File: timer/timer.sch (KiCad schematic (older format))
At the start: 23 parts, among them J1 Conn_01x02_Female, Q1 BC546, Q2 BC546, U1 LM339, U2 7402

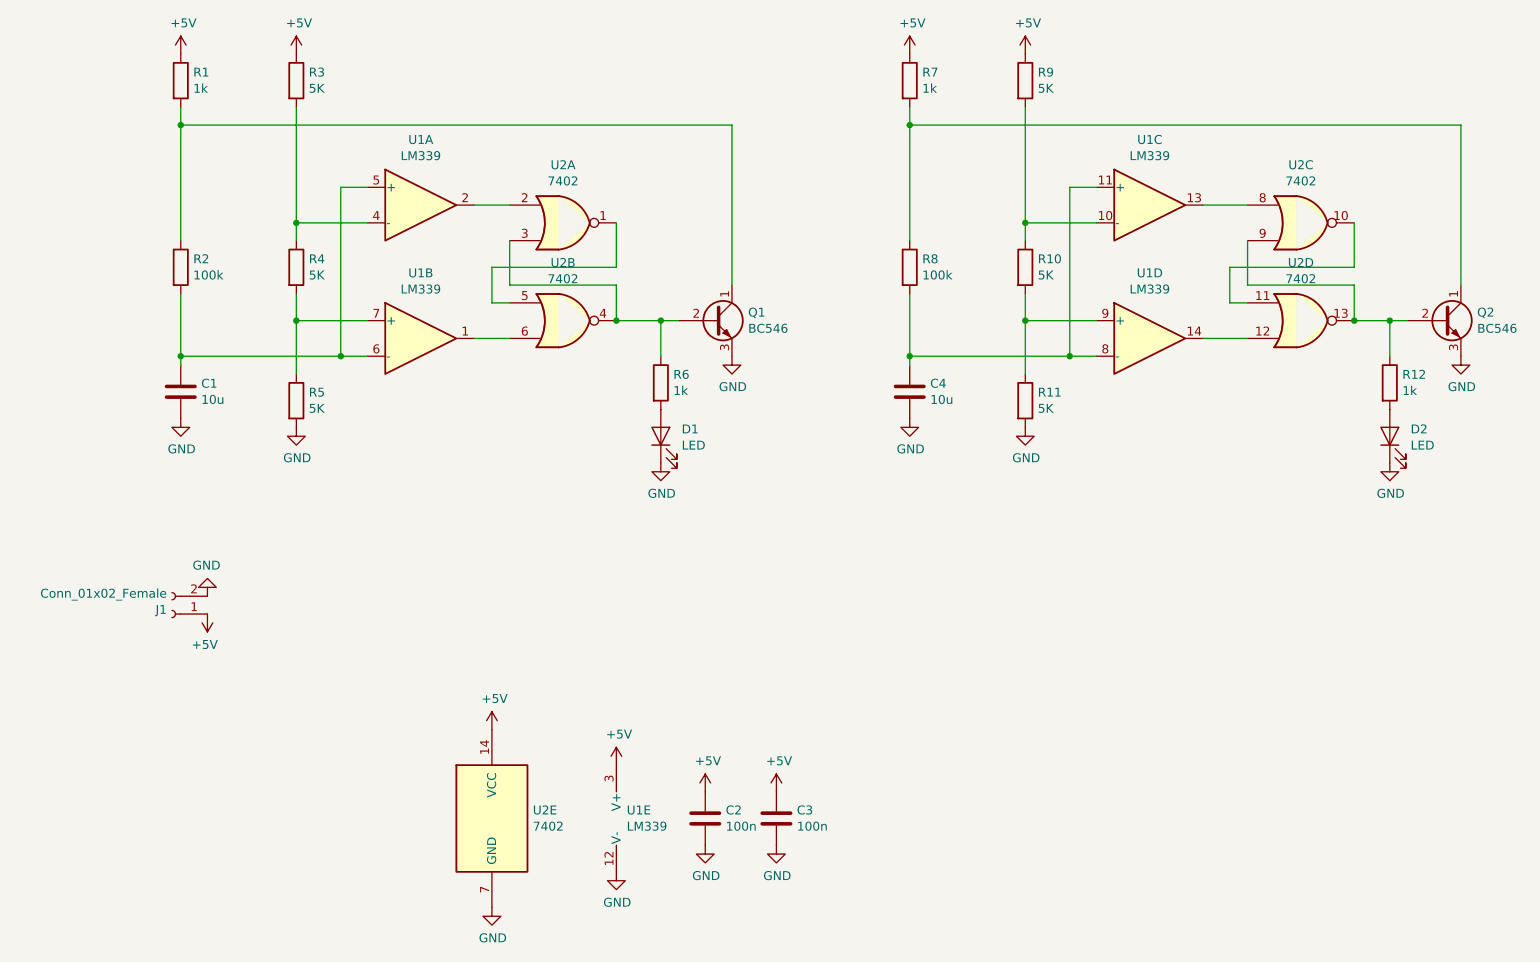
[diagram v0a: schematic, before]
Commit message: Start using opamp that can ouput stuff
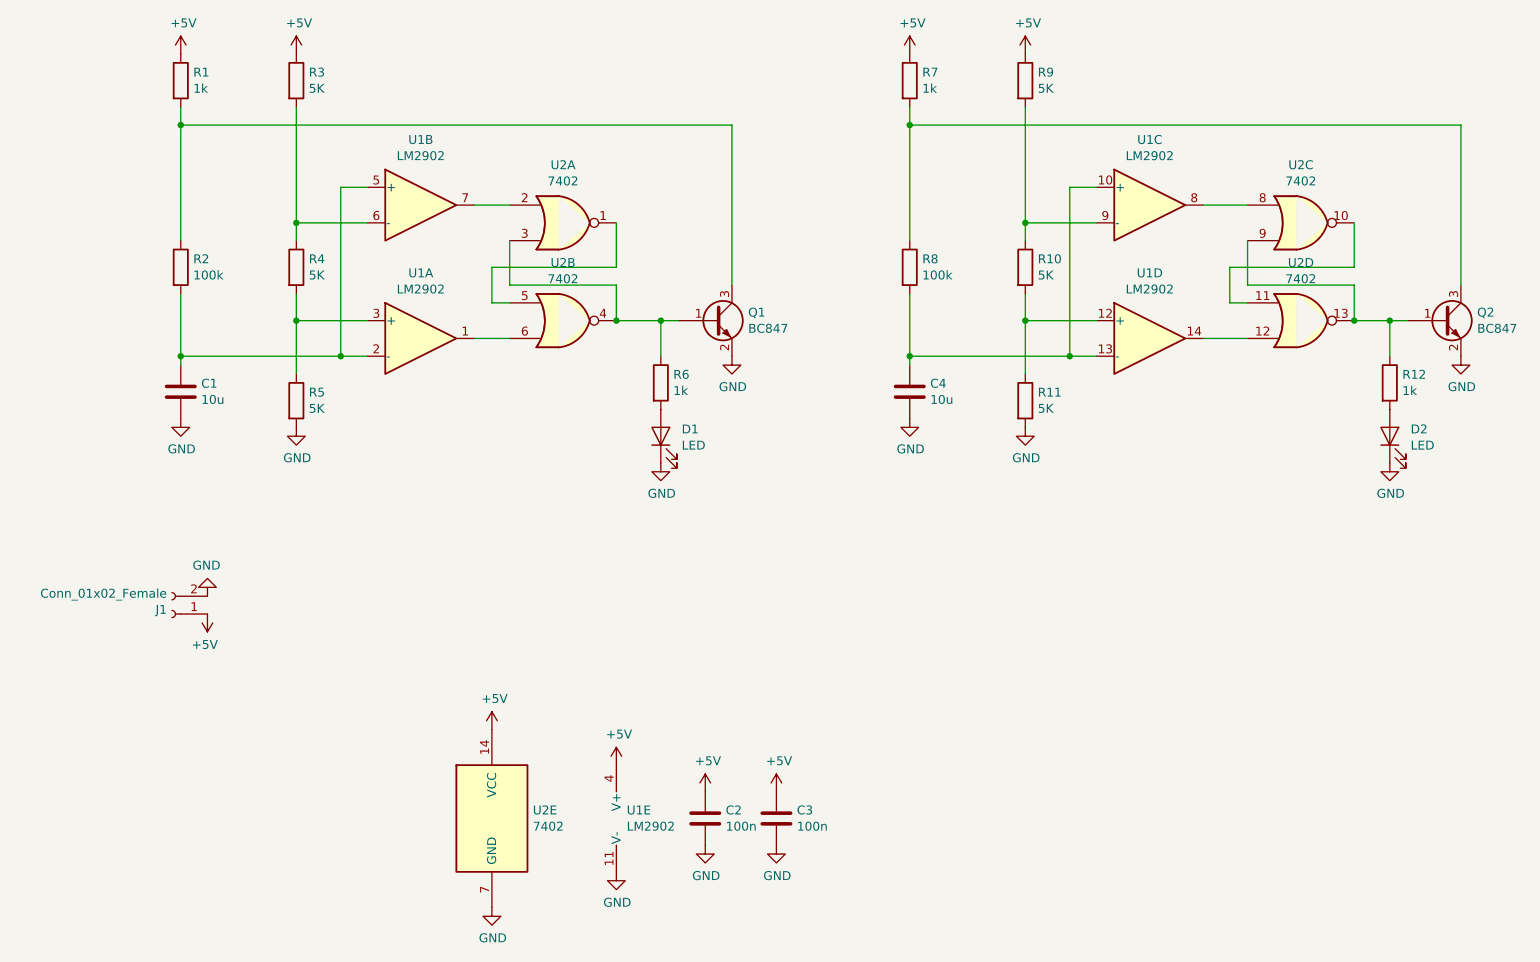
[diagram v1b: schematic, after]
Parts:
- removed Q1, Q2: BC546, Package_TO_SOT_THT:TO-92_Inline, symbol Transistor_BJT:BC546
- removed U1: LM339, Package_DIP:DIP-14_W7.62mm, symbol Comparator:LM339
- added Q1, Q2: BC847, Package_TO_SOT_SMD:SOT-323_SC-70_Handsoldering, symbol Device:Q_NPN_BEC
- added U1: LM2902, Package_SO:TSSOP-14_4.4x5mm_P0.65mm, symbol Amplifier_Operational:LM2902
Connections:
- net +5V: now also U1.4 (V+)
- net GND: now also Q1.2 (E), Q2.2 (E), U1.11 (V-)
- net at U2.2: now also U1.7
- net at R6.1, U2.3, U2.4: now also Q1.1 (B)
- net at U2.6: now also U1.1
- net at U2.8: now also U1.8
- net at R12.1, U2.13, U2.9: now also Q2.1 (B)
- net at U2.12: now also U1.14
- net at R3.2, R4.1: now also U1.6 (-)
- net at C1.1, R2.2: now also U1.2 (-), U1.5 (+)
- net at R4.2, R5.1: now also U1.3 (+)
- net at R10.1, R9.2: now also U1.9 (-)
- net at C4.1, R8.2: now also U1.10 (+), U1.13 (-)
- net at R10.2, R11.1: now also U1.12 (+)
- net at R1.2, R2.1: now also Q1.3 (C)
- net at R7.2, R8.1: now also Q2.3 (C)
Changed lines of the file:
@@
-$EndComp
-$Comp
-L Comparator:LM339 U1
-U 1 1 605E8C8D
-P 2950 2950
-F 0 "U1" H 2950 3317 50  0000 C CNN
-F 1 "LM339" H 2950 3226 50  0000 C CNN
-F 2 "Package_DIP:DIP-14_W7.62mm" H 2900 3050 50  0001 C CNN
-F 3 "https://www.st.com/resource/en/datasheet/lm139.pdf" H 3000 3150 50  0001 C CNN
-	1    2950 2950
-	1    0    0    -1
-$EndComp
-$Comp
-L Comparator:LM339 U1
-U 2 1 605E91D7
-P 2950 3700
-F 0 "U1" H 2950 4067 50  0000 C CNN
-F 1 "LM339" H 2950 3976 50  0000 C CNN
-F 2 "Package_DIP:DIP-14_W7.62mm" H 2900 3800 50  0001 C CNN
-F 3 "https://www.st.com/resource/en/datasheet/lm139.pdf" H 3000 3900 50  0001 C CNN
-	2    2950 3700
-	1    0    0    -1
-$EndComp
-$Comp
-L Comparator:LM339 U1
-U 3 1 605EA1D7
-P 7050 2950
-F 0 "U1" H 7050 3317 50  0000 C CNN
-F 1 "LM339" H 7050 3226 50  0000 C CNN
-F 2 "Package_DIP:DIP-14_W7.62mm" H 7000 3050 50  0001 C CNN
-F 3 "https://www.st.com/resource/en/datasheet/lm139.pdf" H 7100 3150 50  0001 C CNN
-	3    7050 2950
-	1    0    0    -1
-$EndComp
-$Comp
-L Comparator:LM339 U1
-U 4 1 605EAA55
-P 7050 3700
-F 0 "U1" H 7050 4067 50  0000 C CNN
-F 1 "LM339" H 7050 3976 50  0000 C CNN
-F 2 "Package_DIP:DIP-14_W7.62mm" H 7000 3800 50  0001 C CNN
-F 3 "https://www.st.com/resource/en/datasheet/lm139.pdf" H 7100 3900 50  0001 C CNN
-	4    7050 3700
-	1    0    0    -1
-$EndComp
-$Comp
-L Comparator:LM339 U1
-U 5 1 605EB171
-P 4150 6400
-F 0 "U1" H 4108 6446 50  0000 L CNN
-F 1 "LM339" H 4108 6355 50  0000 L CNN
-F 2 "Package_DIP:DIP-14_W7.62mm" H 4100 6500 50  0001 C CNN
-F 3 "https://www.st.com/resource/en/datasheet/lm139.pdf" H 4200 6600 50  0001 C CNN
-	5    4150 6400
-	1    0    0    -1
-$EndComp
-$Comp
-L Transistor_BJT:BC546 Q1
-U 1 1 605EC241
-P 4600 3600
-F 0 "Q1" H 4791 3646 50  0000 L CNN
-F 1 "BC546" H 4791 3555 50  0000 L CNN
-F 2 "Package_TO_SOT_THT:TO-92_Inline" H 4800 3525 50  0001 L CIN
-F 3 "http://www.fairchildsemi.com/ds/BC/BC547.pdf" H 4600 3600 50  0001 L CNN
-	1    4600 3600
-	1    0    0    -1
 $EndComp
 $Comp
@@
 $EndComp
 $Comp
-L Transistor_BJT:BC546 Q2
-U 1 1 60644E3F
-P 8700 3600
-F 0 "Q2" H 8891 3646 50  0000 L CNN
-F 1 "BC546" H 8891 3555 50  0000 L CNN
-F 2 "Package_TO_SOT_THT:TO-92_Inline" H 8900 3525 50  0001 L CIN
-F 3 "http://www.fairchildsemi.com/ds/BC/BC547.pdf" H 8700 3600 50  0001 L CNN
-	1    8700 3600
-	1    0    0    -1
-$EndComp
-$Comp
 L Device:R R9
 U 1 1 60644E45
@@
 	-1   0    0    1
 $EndComp
+$Comp
+L Amplifier_Operational:LM2902 U1
+U 1 1 605F6E50
+P 2950 3700
+F 0 "U1" H 2950 4067 50  0000 C CNN
+F 1 "LM2902" H 2950 3976 50  0000 C CNN
+F 2 "Package_SO:TSSOP-14_4.4x5mm_P0.65mm" H 2900 3800 50  0001 C CNN
+F 3 "http://www.ti.com/lit/ds/symlink/lm2902-n.pdf" H 3000 3900 50  0001 C CNN
+	1    2950 3700
+	1    0    0    -1
+$EndComp
+$Comp
+L Amplifier_Operational:LM2902 U1
+U 2 1 605F8407
+P 2950 2950
+F 0 "U1" H 2950 3317 50  0000 C CNN
+F 1 "LM2902" H 2950 3226 50  0000 C CNN
+F 2 "Package_SO:TSSOP-14_4.4x5mm_P0.65mm" H 2900 3050 50  0001 C CNN
+F 3 "http://www.ti.com/lit/ds/symlink/lm2902-n.pdf" H 3000 3150 50  0001 C CNN
+	2    2950 2950
+	1    0    0    -1
+$EndComp
+$Comp
+L Amplifier_Operational:LM2902 U1
+U 3 1 605F9DD5
+P 7050 2950
+F 0 "U1" H 7050 3317 50  0000 C CNN
+F 1 "LM2902" H 7050 3226 50  0000 C CNN
+F 2 "Package_SO:TSSOP-14_4.4x5mm_P0.65mm" H 7000 3050 50  0001 C CNN
+F 3 "http://www.ti.com/lit/ds/symlink/lm2902-n.pdf" H 7100 3150 50  0001 C CNN
+	3    7050 2950
+	1    0    0    -1
+$EndComp
+$Comp
+L Amplifier_Operational:LM2902 U1
+U 4 1 605FAEBE
+P 7050 3700
+F 0 "U1" H 7050 4067 50  0000 C CNN
+F 1 "LM2902" H 7050 3976 50  0000 C CNN
+F 2 "Package_SO:TSSOP-14_4.4x5mm_P0.65mm" H 7000 3800 50  0001 C CNN
+F 3 "http://www.ti.com/lit/ds/symlink/lm2902-n.pdf" H 7100 3900 50  0001 C CNN
+	4    7050 3700
+	1    0    0    -1
+$EndComp
+$Comp
+L Amplifier_Operational:LM2902 U1
+U 5 1 605FBE50
+P 4150 6400
+F 0 "U1" H 4108 6446 50  0000 L CNN
+F 1 "LM2902" H 4108 6355 50  0000 L CNN
+F 2 "Package_SO:TSSOP-14_4.4x5mm_P0.65mm" H 4100 6500 50  0001 C CNN
+F 3 "http://www.ti.com/lit/ds/symlink/lm2902-n.pdf" H 4200 6600 50  0001 C CNN
+	5    4150 6400
+	1    0    0    -1
+$EndComp
+$Comp
+L Device:Q_NPN_BEC Q1
+U 1 1 60648F70
+P 4600 3600
+F 0 "Q1" H 4791 3646 50  0000 L CNN
+F 1 "BC847" H 4791 3555 50  0000 L CNN
+F 2 "Package_TO_SOT_SMD:SOT-323_SC-70_Handsoldering" H 4800 3700 50  0001 C CNN
+F 3 "~" H 4600 3600 50  0001 C CNN
+	1    4600 3600
+	1    0    0    -1
+$EndComp
+$Comp
+L Device:Q_NPN_BEC Q2
+U 1 1 60649B87
+P 8700 3600
+F 0 "Q2" H 8891 3646 50  0000 L CNN
+F 1 "BC847" H 8891 3555 50  0000 L CNN
+F 2 "Package_TO_SOT_SMD:SOT-323_SC-70_Handsoldering" H 8900 3700 50  0001 C CNN
+F 3 "~" H 8700 3600 50  0001 C CNN
+	1    8700 3600
+	1    0    0    -1
+$EndComp
 $EndSCHEMATC
